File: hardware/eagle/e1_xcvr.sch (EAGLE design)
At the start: 40 parts

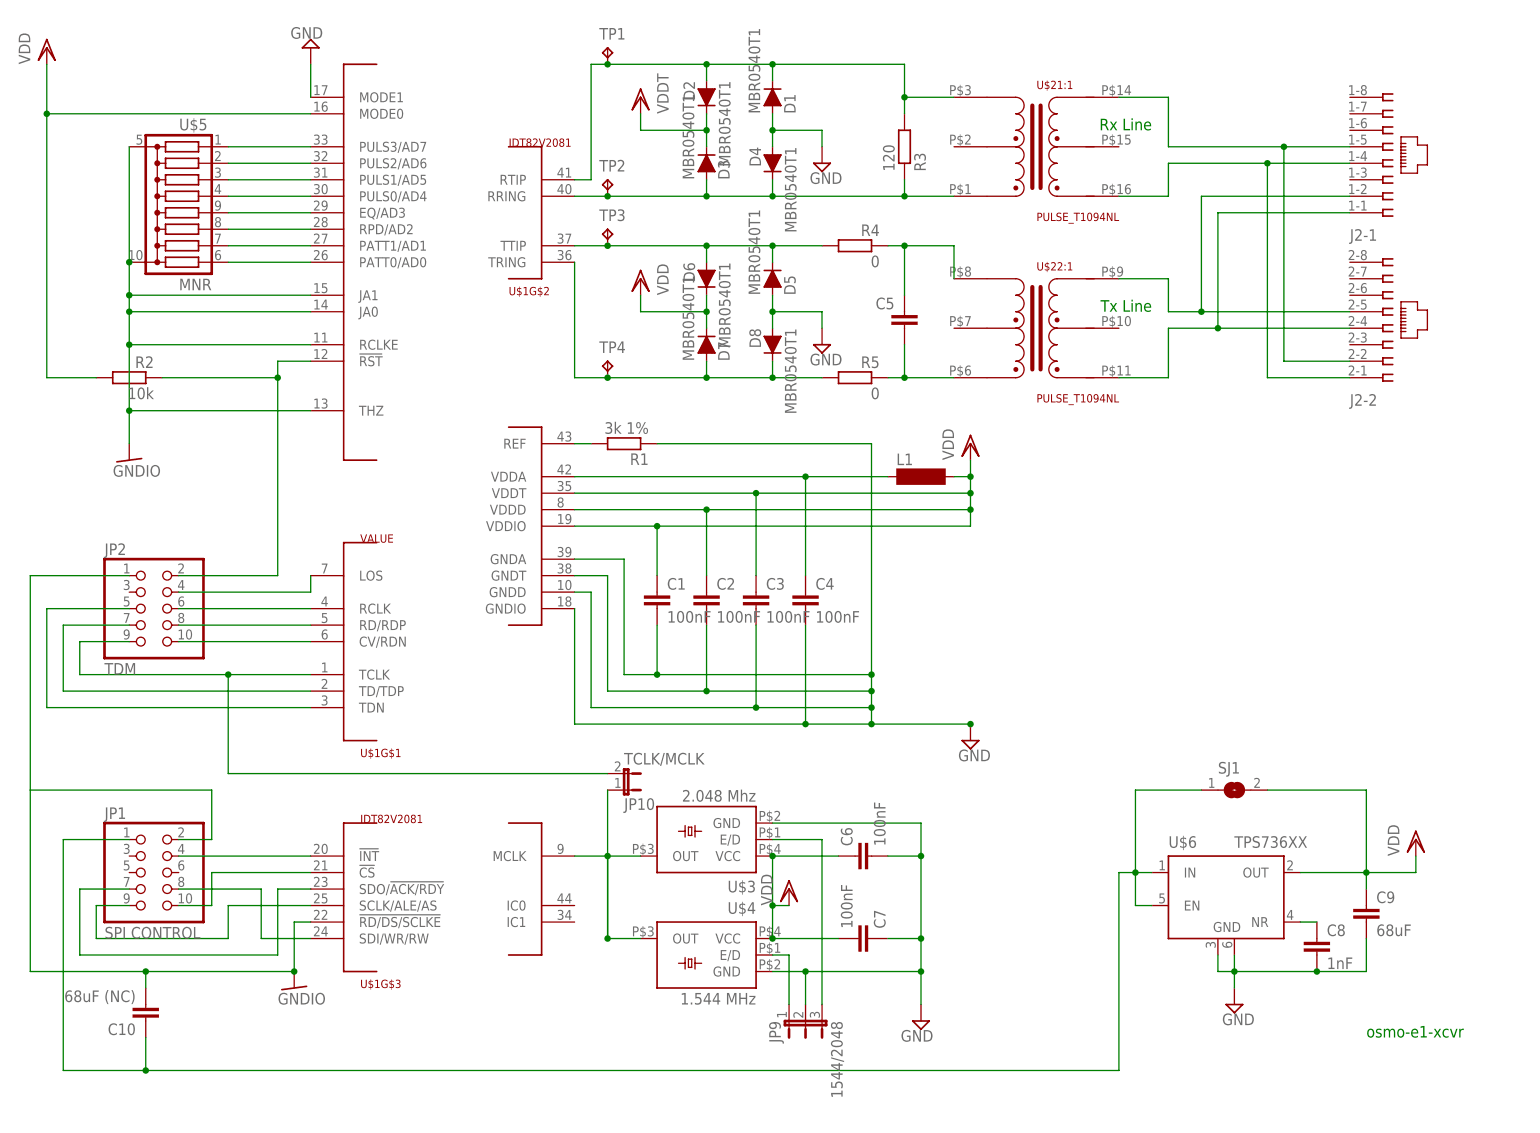
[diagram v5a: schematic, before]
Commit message: add two LEDs (power and LOS) plus required transistor
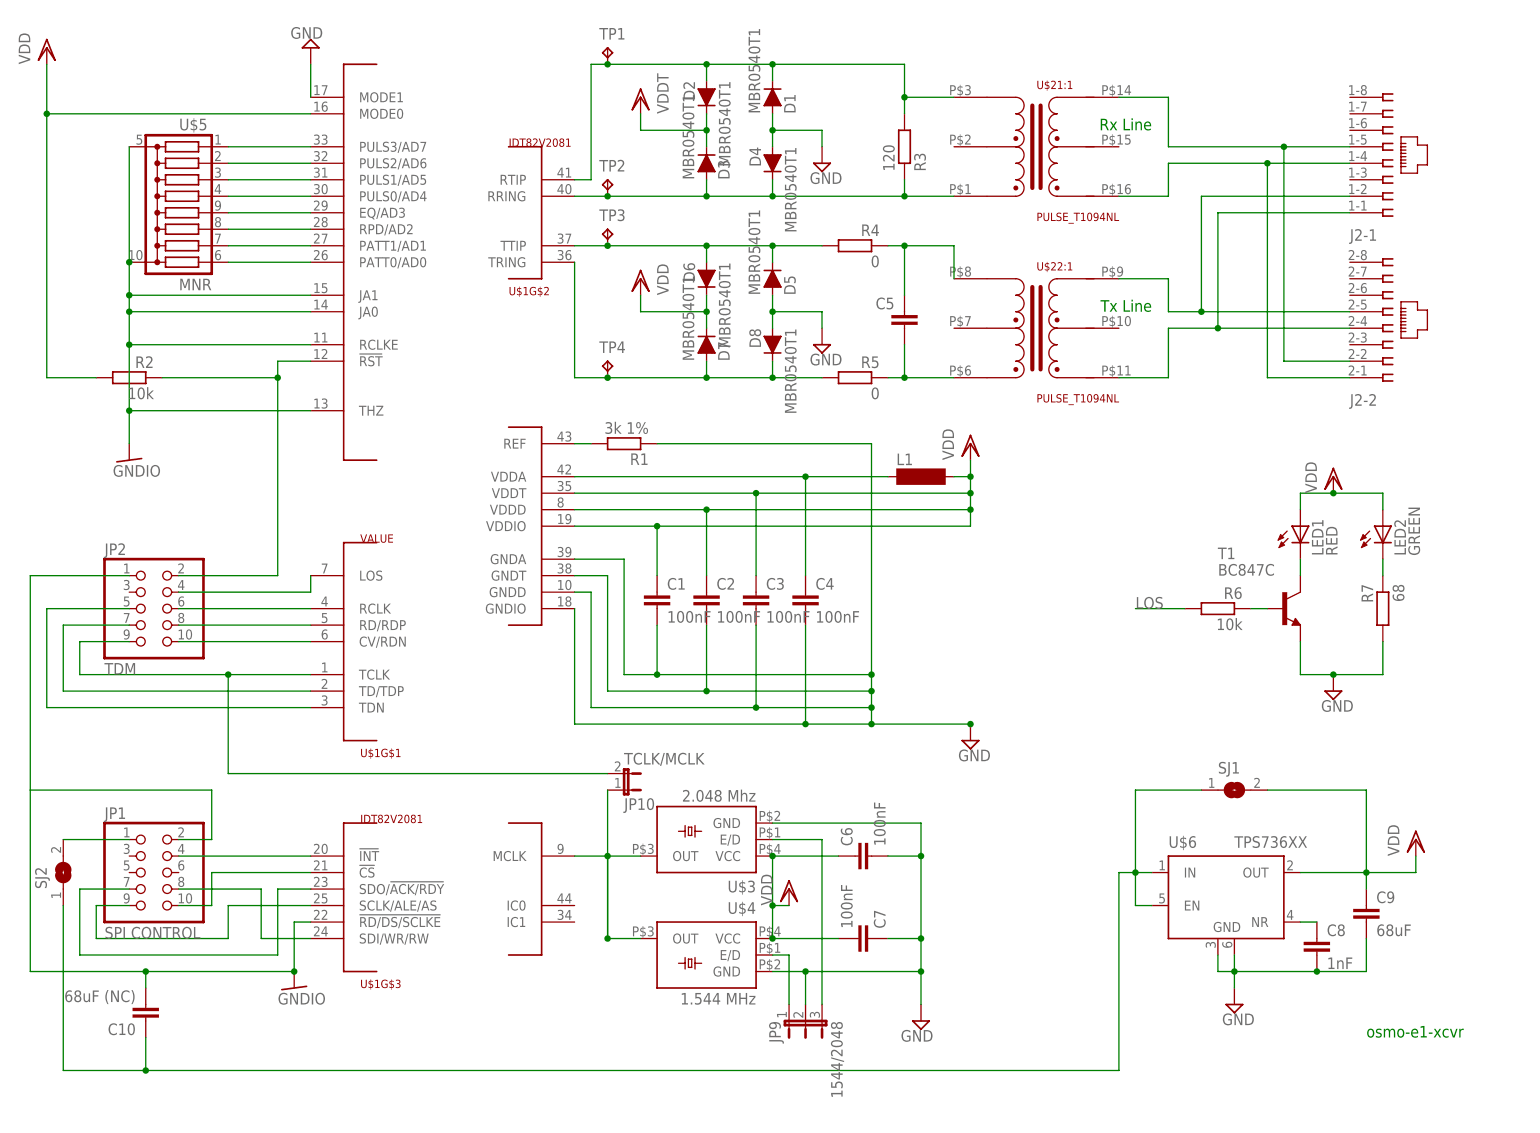
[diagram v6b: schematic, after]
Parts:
- added LED1: RED, led:LEDCHIPLED_0805
- added LED2: GREEN, led:LEDCHIPLED_0805
- added R6: 10k, rcl:R-EU_R0603
- added R7: 68, rcl:R-EU_R0603
- added SJ2: (no value), jumper:SJ
- added T1: BC847C, transistor:BC847C-NPN-SOT23-BEC
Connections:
- removed net N$5: JP2.4, U$1G$1.LOS
- new net LOS: JP2.4, R6.2, U$1G$1.LOS
- new net N$25: LED1.C, T1.C
- new net N$26: R6.1, T1.B
- new net N$30: LED2.C, R7.1
- new net N$7: JP1.1, SJ2.2
- net GND: now also R7.2, T1.E
- net VDD: now also LED1.A, LED2.A
- net VIN: now also SJ2.1; no longer JP1.1
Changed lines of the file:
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@@
 <part name="TP4" library="testpad" deviceset="TP" device="PAD1-13"/>
 <part name="SJ1" library="jumper" deviceset="SJ" device=""/>
+<part name="SJ2" library="jumper" deviceset="SJ" device=""/>
+<part name="LED1" library="led" deviceset="LED" device="CHIPLED_0805" value="RED"/>
+<part name="T1" library="transistor" deviceset="*-NPN-" device="SOT23-BEC" technology="BC847C" value="BC847C"/>
+<part name="R6" library="rcl" deviceset="R-EU_" device="R0603" value="10k"/>
+<part name="LED2" library="led" deviceset="LED" device="CHIPLED_0805" value="GREEN"/>
+<part name="VDD4" library="supply1" deviceset="VDD" device=""/>
+<part name="R7" library="rcl" deviceset="R-EU_" device="R0603" value="68"/>
+<part name="SUPPLY7" library="supply2" deviceset="GND" device=""/>
 </parts>
 <sheets>
@@
 <instance part="TP4" gate="G$1" x="83.82" y="160.02"/>
 <instance part="SJ1" gate="1" x="180.34" y="93.98"/>
+<instance part="SJ2" gate="1" x="0" y="81.28" rot="R90"/>
+<instance part="LED1" gate="G$1" x="190.5" y="134.62"/>
+<instance part="T1" gate="G$1" x="187.96" y="121.92"/>
+<instance part="R6" gate="G$1" x="177.8" y="121.92" rot="MR0"/>
+<instance part="LED2" gate="G$1" x="203.2" y="134.62"/>
+<instance part="VDD4" gate="G$1" x="195.58" y="142.24"/>
+<instance part="R7" gate="G$1" x="203.2" y="121.92" rot="MR270"/>
+<instance part="SUPPLY7" gate="GND" x="195.58" y="109.22"/>
 </instances>
 <busses>
@@
 <wire x1="22.86" y1="86.36" x2="17.78" y2="86.36" width="0.1524" layer="91"/>
 </segment>
+<segment>
+<pinref part="T1" gate="G$1" pin="E"/>
+<wire x1="190.5" y1="116.84" x2="190.5" y2="111.76" width="0.1524" layer="91"/>
+<pinref part="R7" gate="G$1" pin="2"/>
+<wire x1="203.2" y1="116.84" x2="203.2" y2="111.76" width="0.1524" layer="91"/>
+<wire x1="203.2" y1="111.76" x2="195.58" y2="111.76" width="0.1524" layer="91"/>
+<pinref part="SUPPLY7" gate="GND" pin="GND"/>
+<wire x1="195.58" y1="111.76" x2="190.5" y2="111.76" width="0.1524" layer="91"/>
+<junction x="195.58" y="111.76"/>
+</segment>
 </net>
 <net name="N$1" class="0">
@@
 <wire x1="200.66" y1="93.98" x2="200.66" y2="81.28" width="0.1524" layer="91"/>
 </segment>
+<segment>
+<pinref part="LED1" gate="G$1" pin="A"/>
+<wire x1="190.5" y1="137.16" x2="190.5" y2="139.7" width="0.1524" layer="91"/>
+<pinref part="LED2" gate="G$1" pin="A"/>
+<wire x1="203.2" y1="137.16" x2="203.2" y2="139.7" width="0.1524" layer="91"/>
+<wire x1="203.2" y1="139.7" x2="195.58" y2="139.7" width="0.1524" layer="91"/>
+<pinref part="VDD4" gate="G$1" pin="VDD"/>
+<wire x1="195.58" y1="139.7" x2="190.5" y2="139.7" width="0.1524" layer="91"/>
+<junction x="195.58" y="139.7"/>
+</segment>
 </net>
 <net name="GNDIO" class="0">
@@
 </segment>
 </net>
-<net name="N$5" class="0">
-<segment>
-<pinref part="U$1" gate="G$1" pin="LOS"/>
-<wire x1="38.1" y1="127" x2="38.1" y2="124.46" width="0.1524" layer="91"/>
-<pinref part="JP2" gate="A" pin="4"/>
-<wire x1="38.1" y1="124.46" x2="17.78" y2="124.46" width="0.1524" layer="91"/>
-</segment>
-</net>
 <net name="TCLK" class="0">
 <segment>
@@
 <junction x="165.1" y="81.28"/>
 <wire x1="165.1" y1="81.28" x2="162.56" y2="81.28" width="0.1524" layer="91"/>
-<wire x1="0" y1="86.36" x2="0" y2="50.8" width="0.1524" layer="91"/>
 <wire x1="0" y1="50.8" x2="12.7" y2="50.8" width="0.1524" layer="91"/>
 <wire x1="12.7" y1="50.8" x2="162.56" y2="50.8" width="0.1524" layer="91"/>
@@
 <wire x1="12.7" y1="55.88" x2="12.7" y2="50.8" width="0.1524" layer="91"/>
 <junction x="12.7" y="50.8"/>
-<pinref part="JP1" gate="A" pin="1"/>
-<wire x1="0" y1="86.36" x2="10.16" y2="86.36" width="0.1524" layer="91"/>
 <wire x1="165.1" y1="81.28" x2="165.1" y2="93.98" width="0.1524" layer="91"/>
 <pinref part="SJ1" gate="1" pin="1"/>
 <wire x1="165.1" y1="93.98" x2="175.26" y2="93.98" width="0.1524" layer="91"/>
+<pinref part="SJ2" gate="1" pin="1"/>
+<wire x1="0" y1="50.8" x2="0" y2="76.2" width="0.1524" layer="91"/>
 </segment>
 </net>
@@
 </segment>
 </net>
+<net name="N$7" class="1">
+<segment>
+<pinref part="JP1" gate="A" pin="1"/>
+<wire x1="0" y1="86.36" x2="10.16" y2="86.36" width="0.1524" layer="91"/>
+<pinref part="SJ2" gate="1" pin="2"/>
+</segment>
+</net>
+<net name="N$25" class="0">
+<segment>
+<pinref part="LED1" gate="G$1" pin="C"/>
+<pinref part="T1" gate="G$1" pin="C"/>
+<wire x1="190.5" y1="129.54" x2="190.5" y2="127" width="0.1524" layer="91"/>
+</segment>
+</net>
+<net name="N$26" class="0">
+<segment>
+<pinref part="T1" gate="G$1" pin="B"/>
+<pinref part="R6" gate="G$1" pin="1"/>
+<wire x1="185.42" y1="121.92" x2="182.88" y2="121.92" width="0.1524" layer="91"/>
+</segment>
+</net>
+<net name="LOS" class="0">
+<segment>
+<pinref part="R6" gate="G$1" pin="2"/>
+<wire x1="172.72" y1="121.92" x2="165.1" y2="121.92" width="0.1524" layer="91"/>
+<label x="165.1" y="121.92" size="1.778" layer="95"/>
+</segment>
+<segment>
+<pinref part="U$1" gate="G$1" pin="LOS"/>
+<wire x1="38.1" y1="127" x2="38.1" y2="124.46" width="0.1524" layer="91"/>
+<pinref part="JP2" gate="A" pin="4"/>
+<wire x1="38.1" y1="124.46" x2="17.78" y2="124.46" width="0.1524" layer="91"/>
+</segment>
+</net>
+<net name="N$30" class="0">
+<segment>
+<pinref part="LED2" gate="G$1" pin="C"/>
+<pinref part="R7" gate="G$1" pin="1"/>
+<wire x1="203.2" y1="127" x2="203.2" y2="129.54" width="0.1524" layer="91"/>
+</segment>
+</net>

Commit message: re-route complete board, add PWR jumper, LED series resistor
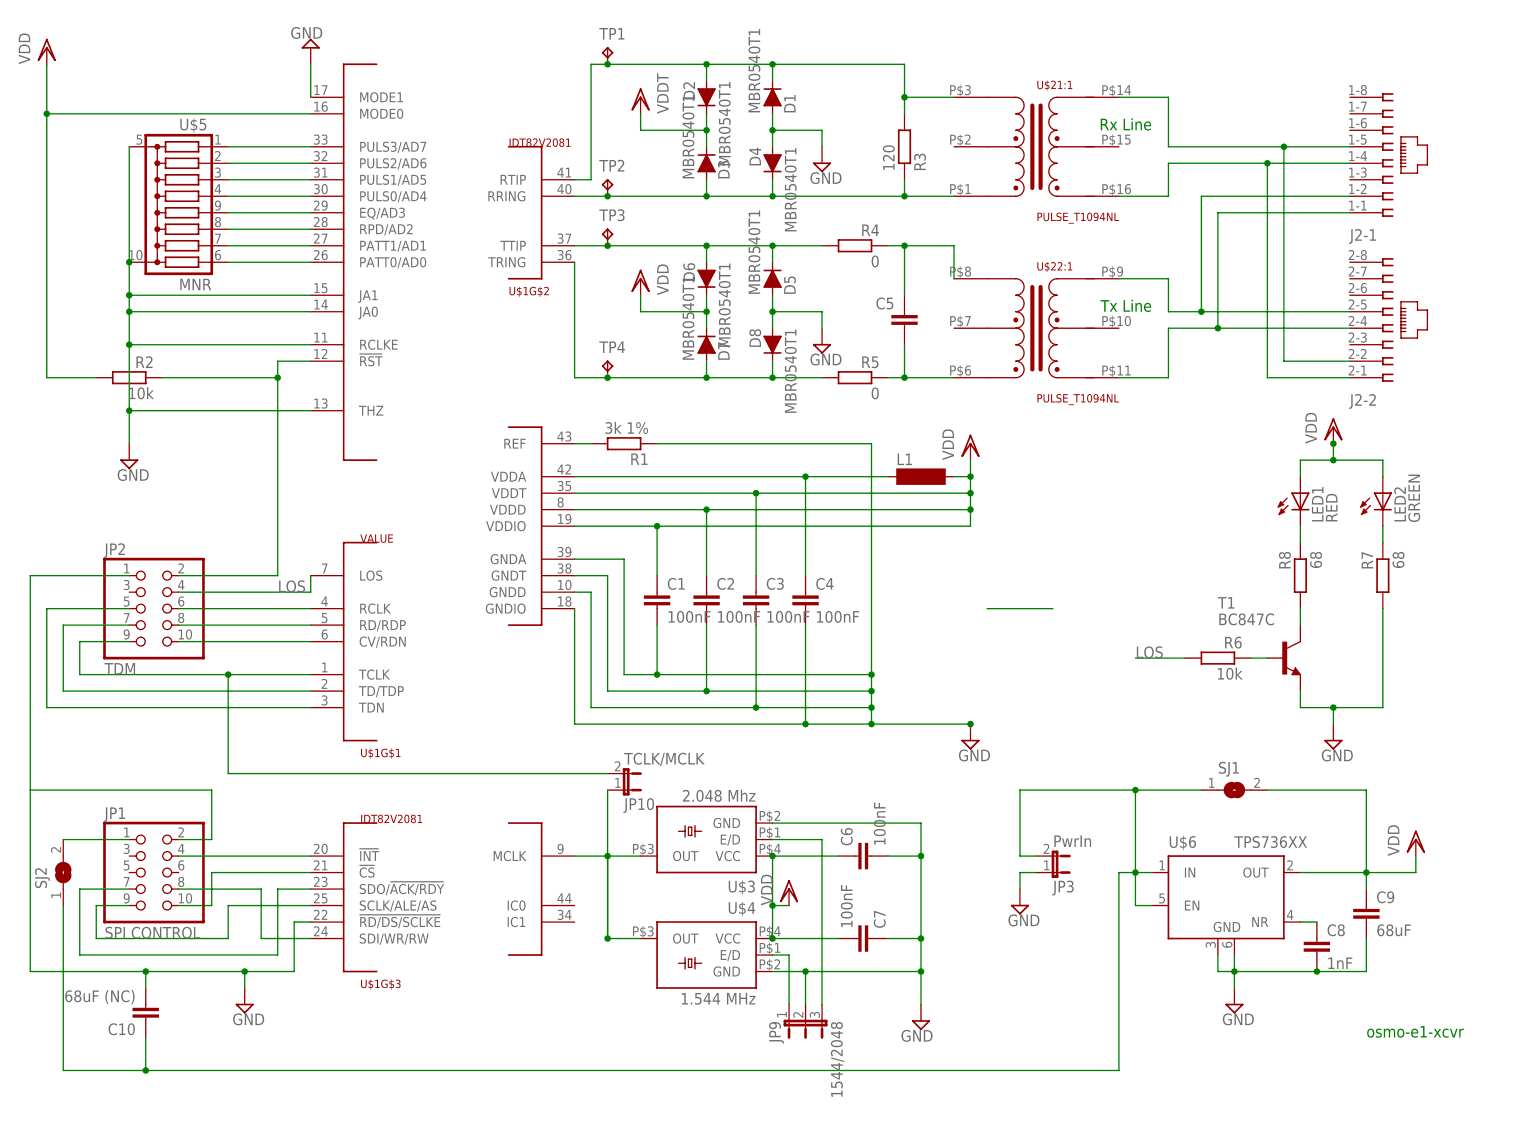
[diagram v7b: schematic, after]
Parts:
- added JP3: PwrIn, jumper:JP1E
- added R8: 68, rcl:R-EU_R0603
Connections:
- removed net GNDIO: U$1G$4.JA0, U$1G$4.JA1, U$1G$4.RCLKE, U$1G$4.THZ, U$5.C, U$5.D
- removed net N$25: LED1.C, T1.C
- new net N$18: R8.2, T1.C
- new net N$5: LED1.C, R8.1
- net GND: now also JP3.1, U$1G$4.JA0, U$1G$4.JA1, U$1G$4.RCLKE, U$1G$4.THZ, U$5.C, U$5.D
- net VIN: now also JP3.2
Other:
- moved on the sheet: LED1, LED2, R6, R7, T1
